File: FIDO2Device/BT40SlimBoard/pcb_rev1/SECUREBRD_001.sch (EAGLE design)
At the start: 32 parts, among them CN1 2137160001, CN2 IF_4PIN, CN4 IF_3PIN_SOL, SW3 SKTADAE010, SW4 SKRPACE010, SW5 SKRPACE010, U1 BT40, U3 ADP122ACPZ-3.3-R7

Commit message: 回路図を更新
・プログラミングI/F部に、リセットピンを追加
（PCA10095からファームウェア書込み時、BT40に対してリセット指示できるようにするための措置）
・一部の部品番号を変更
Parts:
- removed C10, C11: 1uF, Parts:CAP_0603
- removed R6: 1.2k, Parts:RESISTOR_0402
- removed SW4, SW5: SKRPACE010, Parts:SKRPACE010
- added C1, C2: 4.7uF, Parts:CAP_0603
- added R1: 5.1k, Parts:RESISTOR_0402
- added SW1, SW2: SKRPACE010, Parts:SKRPACE010
- C3: value 4.7uF -> 0.01uF; device Parts:CAP_0603 -> Parts:CAP_0402K
- C4: value 4.7uF -> 0.1uF; device Parts:CAP_0603 -> Parts:CAP_0402K
- C5: value 0.01uF -> 0.1uF
- C7, C8: value 0.1uF -> 1uF; device Parts:CAP_0402K -> Parts:CAP_0603
- CN2: value IF_4PIN -> IF_5PIN_H; device Connectors:IF_4PIN -> Connectors:IF_5PIN_H
- R2: value 5.1k -> 1.2k
- renumbered CN4 to CN3, U3 to U2
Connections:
- net 0V: now also C1.2, C2.2, SW1.S, SW1.S1, SW2.S, SW2.S1; no longer C10.2, C11.2, SW4.S, SW4.S1, SW5.S, SW5.S1
- net LED1: now also R2.1; no longer R6.1
- net N$2: now also R1.2; no longer R2.2
- net N$3: now also C7.1; no longer C10.1
- net N$8: now also R2.2; no longer R6.2
- net RESET: now also CN2.5
- net SW1: now also SW1.P, SW1.P1; no longer SW4.P, SW4.P1
- net SW2: now also SW2.P, SW2.P1; no longer SW5.P, SW5.P1
- net USB_GND: now also R1.1; no longer R2.1
- net VBUS: now also C3.1; no longer C8.1
- net VBUS_NRF: now also C2.1, C8.1; no longer C11.1, C7.1
- net VDD_NRF: now also C1.1; no longer C3.1

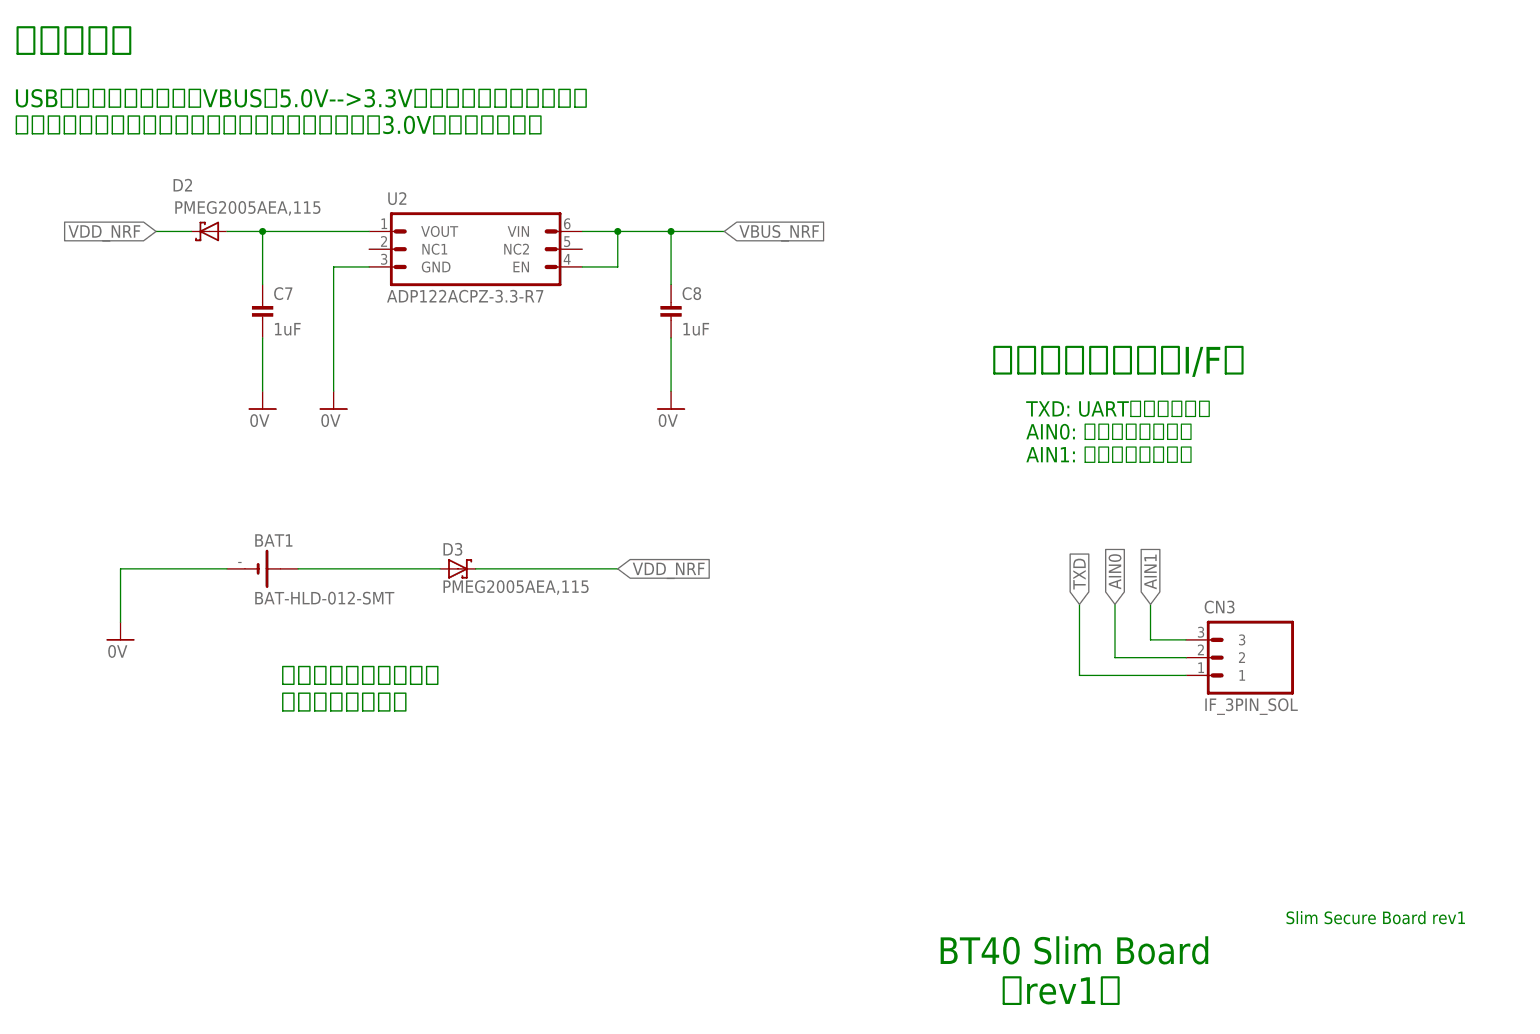
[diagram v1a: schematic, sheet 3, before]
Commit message: 回路図を更新
・VBUS_NRFのバイパスコンデンサーは不要なので削除
・ユーティリティーI/FにGNDピンを追加
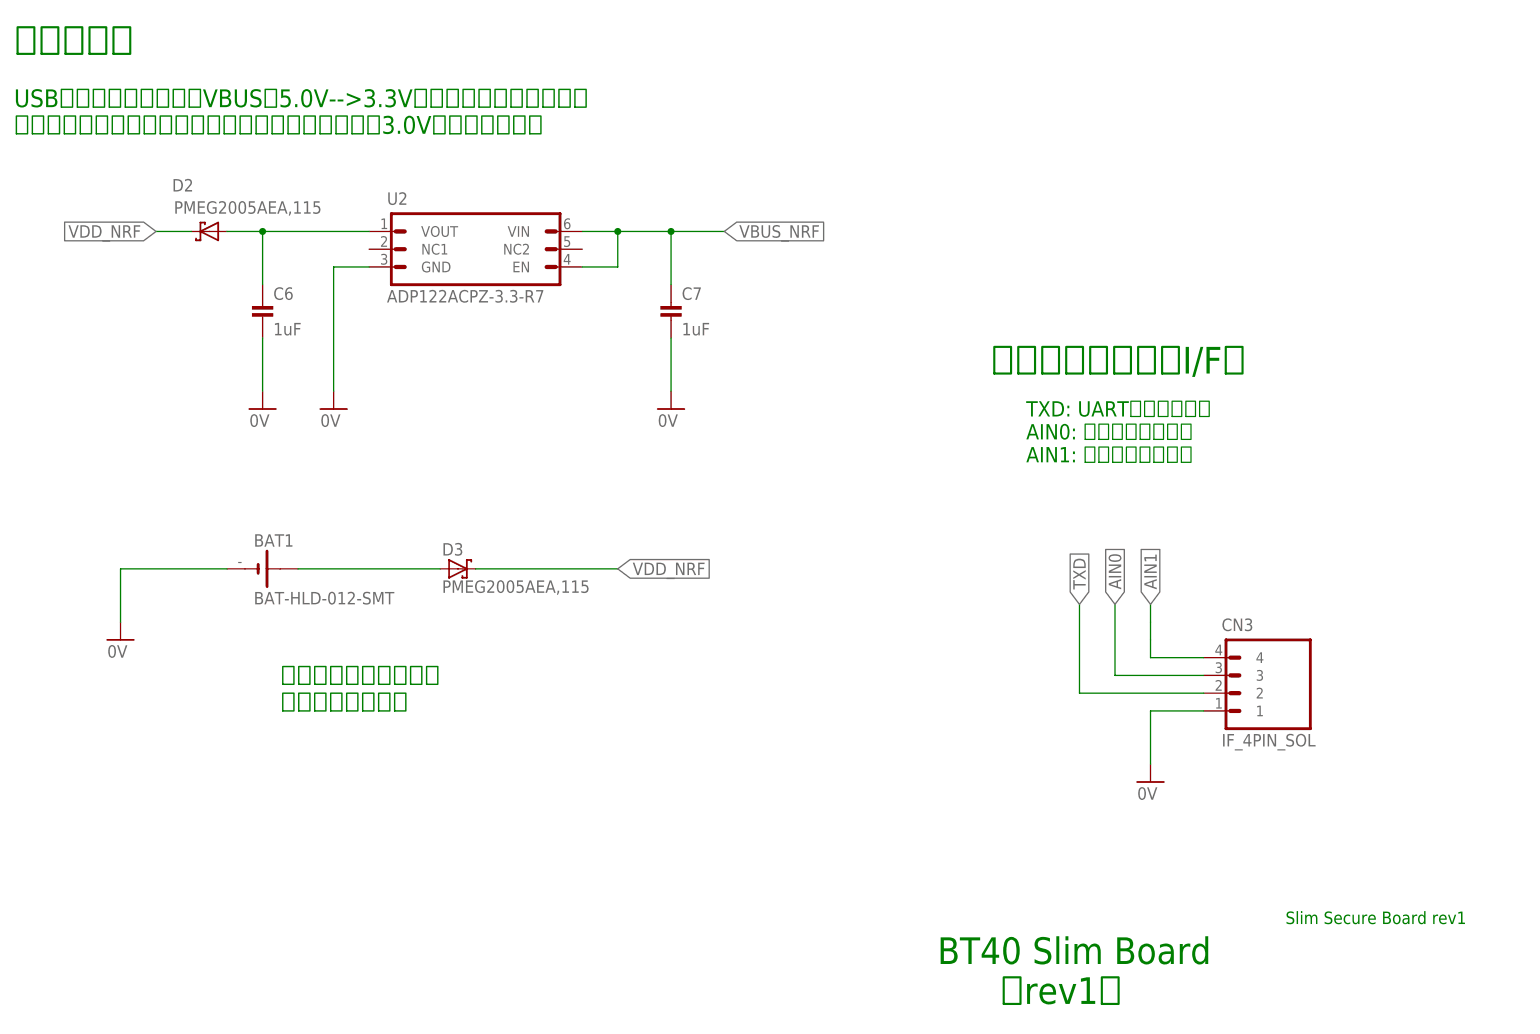
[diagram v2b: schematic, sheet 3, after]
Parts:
- removed C8: 1uF, Parts:CAP_0603
- C2: value 4.7uF -> 0.01uF; device Parts:CAP_0603 -> Parts:CAP_0402K
- C3: value 0.01uF -> 0.1uF
- C5: value 0.1uF -> 10uF; device Parts:CAP_0402K -> Parts:CAP_0603
- C6: value 10uF -> 1uF
- CN3: value IF_3PIN_SOL -> IF_4PIN_SOL; device Connectors:IF_3PIN_SOL -> Connectors:IF_4PIN_SOL
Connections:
- net 0V: now also CN3.1; no longer C8.2
- net AIN0: now also CN3.3; no longer CN3.2
- net AIN1: now also CN3.4; no longer CN3.3
- net N$3: now also C6.1; no longer C7.1
- net TXD: now also CN3.2; no longer CN3.1
- net VBUS: now also C2.1, C4.1; no longer C3.1, C6.1
- net VBUS_NRF: now also C3.1, C7.1; no longer C2.1, C4.1, C8.1
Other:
- moved on the sheet: C1, C3, C4, C5, C7
